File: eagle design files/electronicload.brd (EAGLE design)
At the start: 79.3 x 53.3 mm, 31 parts, among them Q1 IRLB3034PbF, U1 ARDUINO_BLUEPILL, U2 LMV324, X1 ED350/2

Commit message: R2.01 Changed capacitor values.
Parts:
- C5, C6: value 100n -> 1u
- C7: value 1u -> 100n
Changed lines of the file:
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@@
 <attribute name="VALUE" x="43.18" y="31.75" size="1.27" layer="27" ratio="10" rot="R270"/>
 </element>
-<element name="C5" library="rcl" library_urn="urn:adsk.eagle:library:334" package="C0603K" package3d_urn="urn:adsk.eagle:package:23680/2" value="100n" x="24.4" y="18.64" smashed="yes" rot="R270">
+<element name="C5" library="rcl" library_urn="urn:adsk.eagle:library:334" package="C0603K" package3d_urn="urn:adsk.eagle:package:23680/2" value="1u" x="24.4" y="18.64" smashed="yes" rot="R270">
 <attribute name="DIGIKEY" value="445-7456-1-ND" x="24.4" y="18.64" size="1.778" layer="27" rot="R270" display="off"/>
 <attribute name="NAME" x="24.85" y="20.26" size="1.016" layer="25" ratio="17" rot="R90"/>
@@
 <attribute name="VOLTAGE" value="50V" x="24.4" y="18.64" size="1.778" layer="27" rot="R270" display="off"/>
 </element>
-<element name="C7" library="rcl" library_urn="urn:adsk.eagle:library:334" package="C0603K" package3d_urn="urn:adsk.eagle:package:23680/2" value="1u" x="31.47" y="14.4" smashed="yes" rot="R90">
+<element name="C7" library="rcl" library_urn="urn:adsk.eagle:library:334" package="C0603K" package3d_urn="urn:adsk.eagle:package:23680/2" value="100n" x="31.47" y="14.4" smashed="yes" rot="R90">
 <attribute name="DIGIKEY" value="445-12511-1-ND" x="31.47" y="14.4" size="1.778" layer="27" rot="R90" display="off"/>
 <attribute name="NAME" x="33.32" y="13.7" size="1.016" layer="25" ratio="17" rot="R90"/>
@@
 <attribute name="VOLTAGE" value="50V" x="26.184" y="25.104" size="1.778" layer="27" rot="R270" display="off"/>
 </element>
-<element name="C6" library="rcl" library_urn="urn:adsk.eagle:library:334" package="C0603K" package3d_urn="urn:adsk.eagle:package:23680/2" value="100n" x="24.68" y="10.53" smashed="yes" rot="R90">
+<element name="C6" library="rcl" library_urn="urn:adsk.eagle:library:334" package="C0603K" package3d_urn="urn:adsk.eagle:package:23680/2" value="1u" x="24.68" y="10.53" smashed="yes" rot="R90">
 <attribute name="DIGIKEY" value="445-7456-1-ND" x="24.68" y="10.53" size="1.778" layer="27" rot="R90" display="off"/>
 <attribute name="NAME" x="25.13" y="7.33" size="1.016" layer="25" ratio="17" rot="R90"/>

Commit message: R2.02 changed opamp to MCP6004-I/SL
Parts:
- U2: value LMV324 -> MCP6004-I/SL
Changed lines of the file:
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@@
 <?xml version="1.0" encoding="utf-8"?>
 <!DOCTYPE eagle SYSTEM "eagle.dtd">
-<eagle version="8.3.2">
+<eagle version="8.4.1">
 <drawing>
 <settings>
@@
 <param name="dpMaxLengthDifference" value="10mm"/>
 <param name="dpGapFactor" value="2.5"/>
-<param name="checkGrid" value="0"/>
 <param name="checkAngle" value="0"/>
 <param name="checkFont" value="1"/>
 <param name="checkRestrict" value="1"/>
+<param name="checkStop" value="0"/>
 <param name="useDiameter" value="13"/>
 <param name="maxErrors" value="50"/>
@@
 <attribute name="VALUE" x="36.683" y="21.251" size="1.27" layer="27" rot="R270"/>
 </element>
-<element name="U2" library="electronicload" package="SO14" value="LMV324" x="31.188" y="24.212" smashed="yes" rot="R270">
+<element name="U2" library="electronicload" package="SO14" value="MCP6004-I/SL" x="31.188" y="24.212" smashed="yes" rot="R270">
 <attribute name="DIGIKEY" value="" x="31.188" y="24.212" size="1.778" layer="27" rot="R270" display="off"/>
 <attribute name="NAME" x="30.583" y="28.792" size="1.27" layer="25" ratio="17"/>

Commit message: 2.03 Changed mosfet to the much more robust BTS133
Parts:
- Q1: value IRLB3034PbF -> BTS133BKSA1
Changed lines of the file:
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@@
 <attribute name="VOLTAGE" value="16V" x="7.6" y="6.8" size="1.778" layer="27" rot="R90" display="off"/>
 </element>
-<element name="Q1" library="electronicload" package="TO220BV" value="IRLB3034PbF" x="50.8" y="26.67" smashed="yes" rot="R270">
-<attribute name="DIGIKEY" value="IRLB3034PbF" x="50.8" y="26.67" size="1.778" layer="27" rot="R270" display="off"/>
+<element name="Q1" library="electronicload" package="TO220BV" value="BTS133BKSA1" x="50.8" y="26.67" smashed="yes" rot="R270">
+<attribute name="DIGIKEY" value="BTS133BKSA1-ND" x="50.8" y="26.67" size="1.778" layer="27" rot="R270" display="off"/>
+<attribute name="FARNELL_OC" value="2480556" x="50.8" y="26.67" size="1.778" layer="27" rot="R270" display="off"/>
+<attribute name="MOUSER_OC" value="726-BTS133BKSA1" x="50.8" y="26.67" size="1.778" layer="27" rot="R270" display="off"/>
 <attribute name="NAME" x="47.588" y="32.1868" size="1.016" layer="25" ratio="17"/>
 <attribute name="VALUE" x="43.18" y="31.75" size="1.27" layer="27" ratio="10" rot="R270"/>

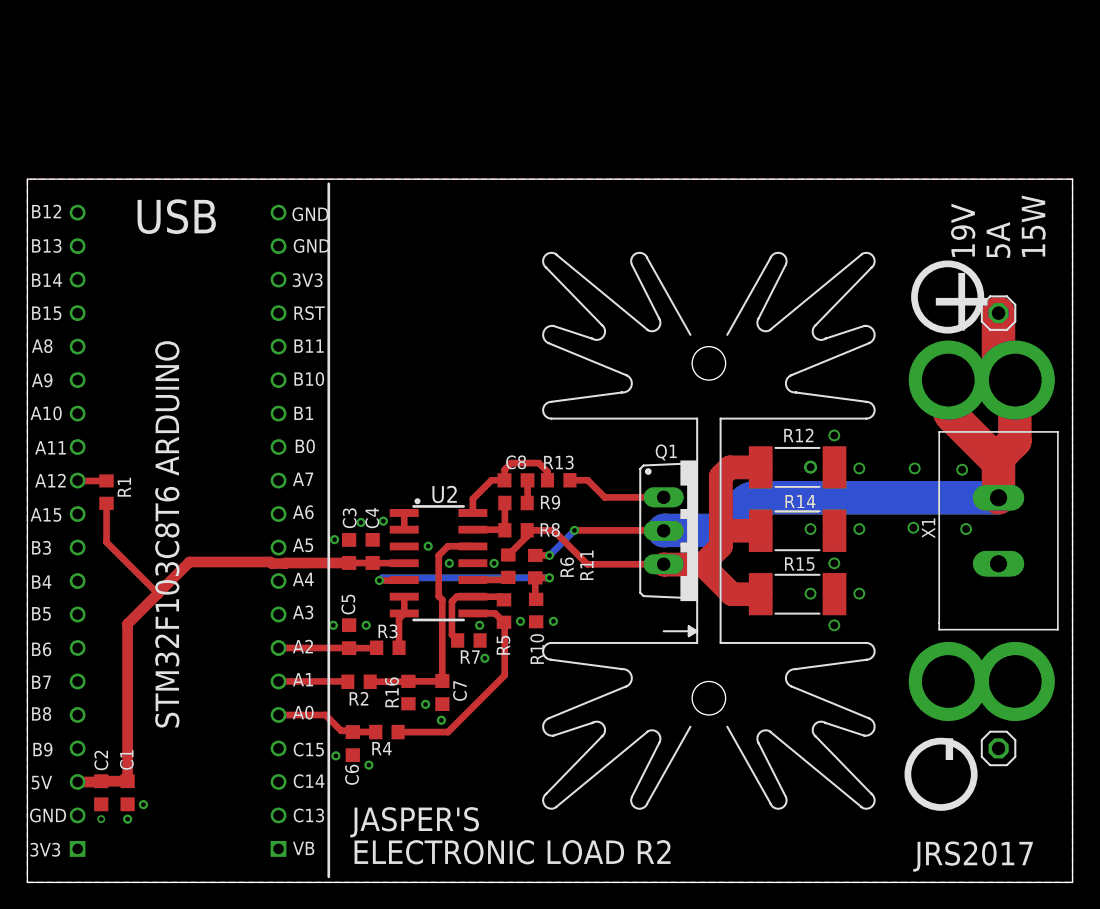
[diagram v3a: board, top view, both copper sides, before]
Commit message: R2.1 New PCB design, added USB connector, changed mosfet from MCP6004 to MCP6074-E/SL
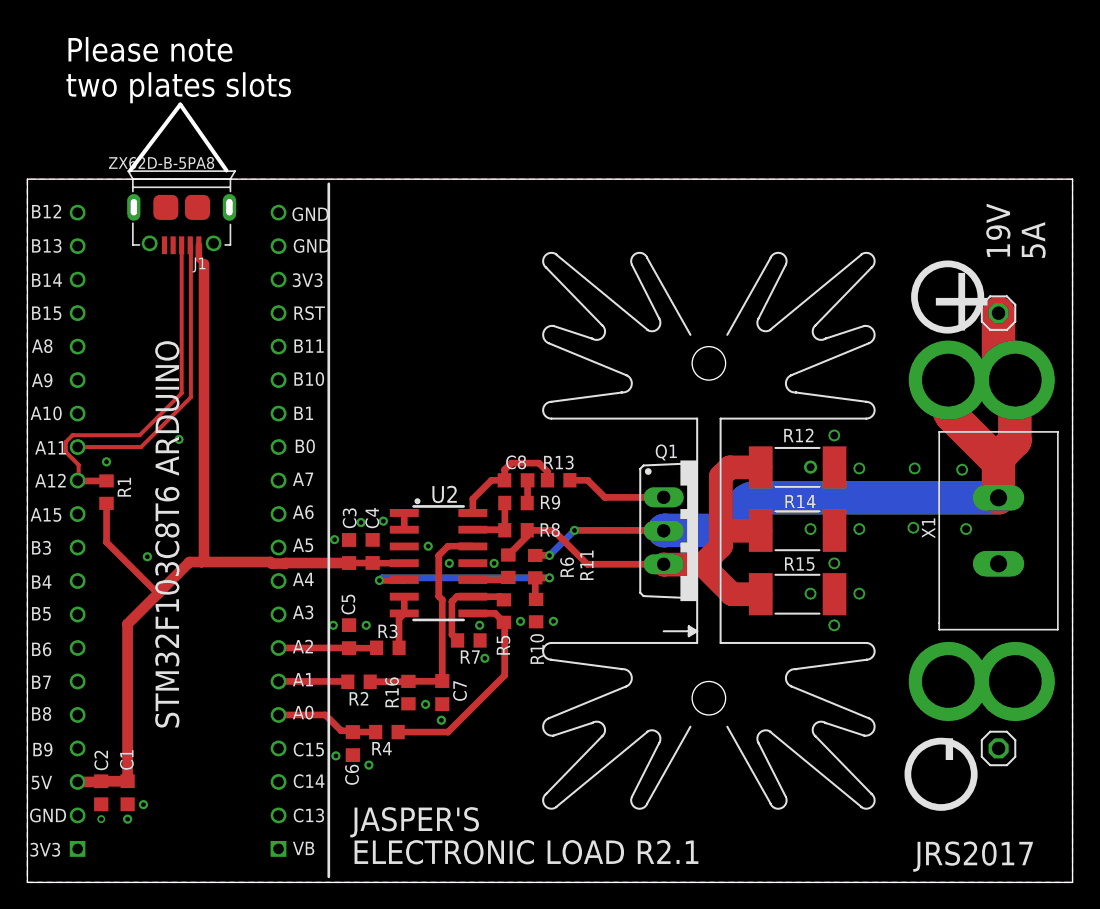
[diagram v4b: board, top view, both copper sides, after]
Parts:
- added J1: ZX62D-B-5PA8, sodaq:MICRO-USB5+6P-SMD-0.65-AB
- U2: value MCP6004-I/SL -> MCP6074-E/SL
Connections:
- new net USB-: J1.2, U1.P$27
- net +5V: now also J1.1
- net GND: now also J1.5, J1.P1, J1.P2, J1.P3, J1.P4, J1.P5, J1.P6
- net USB+: now also J1.3
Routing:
- net USB+: track 2.20 -> 27.1 mm
- net +5V: track 47.3 -> 71.5 mm
- net USB-: track 0.00 -> 21.7 mm
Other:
- board size 79.3 x 53.3 mm -> 79.3 x 59 mm
- board text added: "19V 5A"
- board text added: "ELECTRONIC LOAD R2.1"
- board text added: "Please note two plates slots"
- board text removed: "19V 5A 15W"
- board text removed: "ELECTRONIC LOAD R2"
- board text removed: "USB"
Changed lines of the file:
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@@
 <?xml version="1.0" encoding="utf-8"?>
 <!DOCTYPE eagle SYSTEM "eagle.dtd">
-<eagle version="8.4.1">
+<eagle version="8.5.0">
 <drawing>
 <settings>
@@
 <setting verticaltext="up"/>
 </settings>
-<grid distance="1" unitdist="mm" unit="mm" style="dots" multiple="1" display="yes" altdistance="0.025" altunitdist="inch" altunit="inch"/>
+<grid distance="0.1" unitdist="mm" unit="mm" style="dots" multiple="1" display="yes" altdistance="0.025" altunitdist="inch" altunit="inch"/>
 <layers>
 <layer number="1" name="Top" color="4" fill="1" visible="yes" active="yes"/>
@@
 <layer number="44" name="Drills" color="7" fill="1" visible="yes" active="yes"/>
 <layer number="45" name="Holes" color="7" fill="1" visible="yes" active="yes"/>
-<layer number="46" name="Milling" color="3" fill="1" visible="no" active="yes"/>
+<layer number="46" name="Milling" color="3" fill="1" visible="yes" active="yes"/>
 <layer number="47" name="Measures" color="7" fill="1" visible="no" active="yes"/>
 <layer number="48" name="Document" color="7" fill="1" visible="no" active="yes"/>
@@
 <layer number="59" name="tCarbon" color="7" fill="1" visible="no" active="no"/>
 <layer number="60" name="bCarbon" color="7" fill="1" visible="no" active="no"/>
+<layer number="88" name="SimResults" color="9" fill="1" visible="no" active="no"/>
+<layer number="89" name="SimProbes" color="9" fill="1" visible="no" active="no"/>
 <layer number="90" name="Modules" color="5" fill="1" visible="no" active="no"/>
 <layer number="91" name="Nets" color="2" fill="1" visible="no" active="no"/>
@@
 <text x="66.76" y="11.24" size="5.08" layer="21" ratio="17" rot="R270">-</text>
 <text x="67.3" y="1.3" size="1.778" layer="21" ratio="17">JRS2017</text>
-<text x="24.6" y="1.4" size="1.778" layer="21" ratio="17">ELECTRONIC LOAD R2</text>
+<text x="24.6" y="1.4" size="1.778" layer="21" ratio="17">ELECTRONIC LOAD R2.1</text>
 <text x="11.5" y="11.6" size="1.778" layer="21" ratio="17" rot="R90">STM32F103C8T6 ARDUINO</text>
 <text x="77.2" y="47.2" size="1.778" layer="21" ratio="17" rot="R90">19V
-5A
-15W</text>
+5A</text>
 <circle x="69.8" y="44.4" radius="2.517934375" width="0.508" layer="21"/>
 <circle x="69.3" y="8.2" radius="2.517934375" width="0.508" layer="21"/>
 <text x="24.6" y="3.9" size="1.778" layer="21" ratio="17">JASPER'S</text>
-<text x="11.3" y="50.5" size="2.54" layer="21" ratio="17" align="center">USB</text>
 <wire x1="22.86" y1="52.99" x2="22.86" y2="0.42" width="0.2032" layer="21"/>
+<text x="2.9" y="59.6" size="1.778" layer="46">Please note
+two plates slots</text>
+<wire x1="7.8" y1="54" x2="11.6" y2="59" width="0.3048" layer="46"/>
+<wire x1="11.6" y1="59" x2="15.1" y2="54" width="0.3048" layer="46"/>
 </plain>
 <attributes>
@@
 <param name="checkRestrict" value="1"/>
 <param name="checkStop" value="0"/>
+<param name="checkValues" value="0"/>
 <param name="useDiameter" value="13"/>
 <param name="maxErrors" value="50"/>
@@
 <attribute name="VALUE" x="36.683" y="21.251" size="1.27" layer="27" rot="R270"/>
 </element>
-<element name="U2" library="electronicload" package="SO14" value="MCP6004-I/SL" x="31.188" y="24.212" smashed="yes" rot="R270">
+<element name="U2" library="electronicload" package="SO14" value="MCP6074-E/SL" x="31.188" y="24.212" smashed="yes" rot="R270">
 <attribute name="DIGIKEY" value="" x="31.188" y="24.212" size="1.778" layer="27" rot="R270" display="off"/>
 <attribute name="NAME" x="30.583" y="28.792" size="1.27" layer="25" ratio="17"/>
@@
 <attribute name="NAME" x="28.165" y="13.165" size="1.016" layer="25" ratio="17" rot="R90"/>
 <attribute name="VALUE" x="30.805" y="13.765" size="1.27" layer="27" rot="R90"/>
+</element>
+<element name="J1" library="sodaq" package="MICRO-USB5+6P-SMD-0.65-AB" value="ZX62D-B-5PA8" x="11.7" y="51.2" smashed="yes" rot="R180">
+<attribute name="FARNELL_OC" value="2554981" x="11.7" y="51.2" size="1.778" layer="27" rot="R180" display="off"/>
+<attribute name="MF" value="Hirose" x="11.7" y="51.2" size="1.778" layer="27" rot="R180" display="off"/>
+<attribute name="MPN" value="ZX62D-B-5PA8" x="11.7" y="51.2" size="1.778" layer="27" rot="R180" display="off"/>
+<attribute name="NAME" x="13.605" y="47.39" size="0.889" layer="25" ratio="11" rot="R180"/>
+<attribute name="VALUE" x="14.24" y="55.01" size="0.889" layer="25" ratio="11" rot="R180"/>
 </element>
 </elements>
@@
 <wire x1="9.9" y1="21.9" x2="7.6" y2="19.6" width="0.8128" layer="1"/>
 <wire x1="9.9" y1="21.9" x2="12.3" y2="24.3" width="0.8128" layer="1"/>
-<wire x1="12.3" y1="24.3" x2="18.4348375" y2="24.3" width="0.8128" layer="1"/>
+<wire x1="13.2" y1="24.3" x2="12.3" y2="24.3" width="0.8128" layer="1"/>
+<wire x1="13.2" y1="24.3" x2="18.4348375" y2="24.3" width="0.8128" layer="1"/>
 <wire x1="18.4348375" y1="24.3" x2="18.5476375" y2="24.1872" width="0.8128" layer="1"/>
 <wire x1="18.5476375" y1="24.1872" x2="19.5523625" y2="24.1872" width="0.8128" layer="1"/>
@@
 <wire x1="24.4" y1="24.225" x2="26.18" y2="24.225" width="0.508" layer="1"/>
 <wire x1="26.18" y1="24.225" x2="26.184" y2="24.229" width="0.508" layer="1"/>
+<contactref element="J1" pad="1"/>
+<wire x1="13" y1="48.325" x2="13" y2="47.3" width="0.508" layer="1"/>
+<wire x1="13" y1="47.3" x2="13.4" y2="46.9" width="0.508" layer="1"/>
+<wire x1="13.4" y1="46.9" x2="13.4" y2="24.5" width="0.8128" layer="1"/>
+<wire x1="13.4" y1="24.5" x2="13.2" y2="24.3" width="0.8128" layer="1"/>
 </signal>
 <signal name="N$2">
@@
 <via x="70.9" y="31.3" extent="1-16" drill="0.6"/>
 <via x="71.2" y="26.8" extent="1-16" drill="0.6"/>
+<contactref element="J1" pad="5"/>
+<contactref element="J1" pad="P1"/>
+<contactref element="J1" pad="P6"/>
+<contactref element="J1" pad="P2"/>
+<contactref element="J1" pad="P3"/>
+<contactref element="J1" pad="P4"/>
+<contactref element="J1" pad="P5"/>
+<via x="6" y="31.9" extent="1-16" drill="0.35" diameter="0.7"/>
+<via x="11.5" y="33.6" extent="1-16" drill="0.35" diameter="0.7"/>
+<via x="9.1" y="24.7" extent="1-16" drill="0.35" diameter="0.7"/>
 </signal>
 <signal name="USB+">
 <contactref element="U1" pad="P$28"/>
 <contactref element="R1" pad="1"/>
-<wire x1="6" y1="30.45" x2="3.882425" y2="30.45" width="0.508" layer="1"/>
-<wire x1="3.882425" y1="30.45" x2="3.81" y2="30.48" width="0.508" layer="1" curve="-45"/>
+<wire x1="3.882425" y1="30.45" x2="6" y2="30.45" width="0.508" layer="1"/>
+<wire x1="3.81" y1="30.48" x2="3.882425" y2="30.45" width="0.508" layer="1" curve="45"/>
+<contactref element="J1" pad="3"/>
+<wire x1="11.7" y1="48.325" x2="11.7" y2="37.1" width="0.3048" layer="1"/>
+<wire x1="3.4362125" y1="33.9224" x2="2.9076" y2="33.3937875" width="0.3048" layer="1"/>
+<wire x1="2.9076" y1="33.3937875" x2="2.9076" y2="32.6462125" width="0.3048" layer="1"/>
+<wire x1="8.5224" y1="33.9224" x2="3.4362125" y2="33.9224" width="0.3048" layer="1"/>
+<wire x1="2.9076" y1="32.6462125" x2="3.882425" y2="31.6713875" width="0.3048" layer="1"/>
+<wire x1="3.882425" y1="31.6713875" x2="3.882425" y2="30.45" width="0.3048" layer="1"/>
+<wire x1="11.7" y1="37.1" x2="8.5224" y2="33.9224" width="0.3048" layer="1"/>
+</signal>
+<signal name="USB-">
+<contactref element="U1" pad="P$27"/>
+<contactref element="J1" pad="2"/>
+<wire x1="3.81" y1="33.02" x2="8.62" y2="33.02" width="0.3048" layer="1"/>
+<wire x1="8.62" y1="33.02" x2="12.4" y2="36.8" width="0.3048" layer="1"/>
+<wire x1="12.4" y1="36.8" x2="12.4" y2="48.275" width="0.3048" layer="1"/>
+<wire x1="12.4" y1="48.275" x2="12.35" y2="48.325" width="0.3048" layer="1"/>
 </signal>
 </signals>
